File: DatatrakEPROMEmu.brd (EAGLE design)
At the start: 151.1 x 66 mm, 46 parts, among them IC1 LD1117AS33TR, IC2 XC95144XL_TQ144_P, Q1 BC847CSMD, Q2 BC847CSMD, Q3 BC847CSMD, U1 SN74LVCH16T245DGGR, U2 SN74LVCH16T245DGGR, U3 SN74LVCH16T245DGGR, U4 IS62WV25616DBLL-45TLI, U5 FT240XS, X1 MABC48B2, X2 PN61729-S

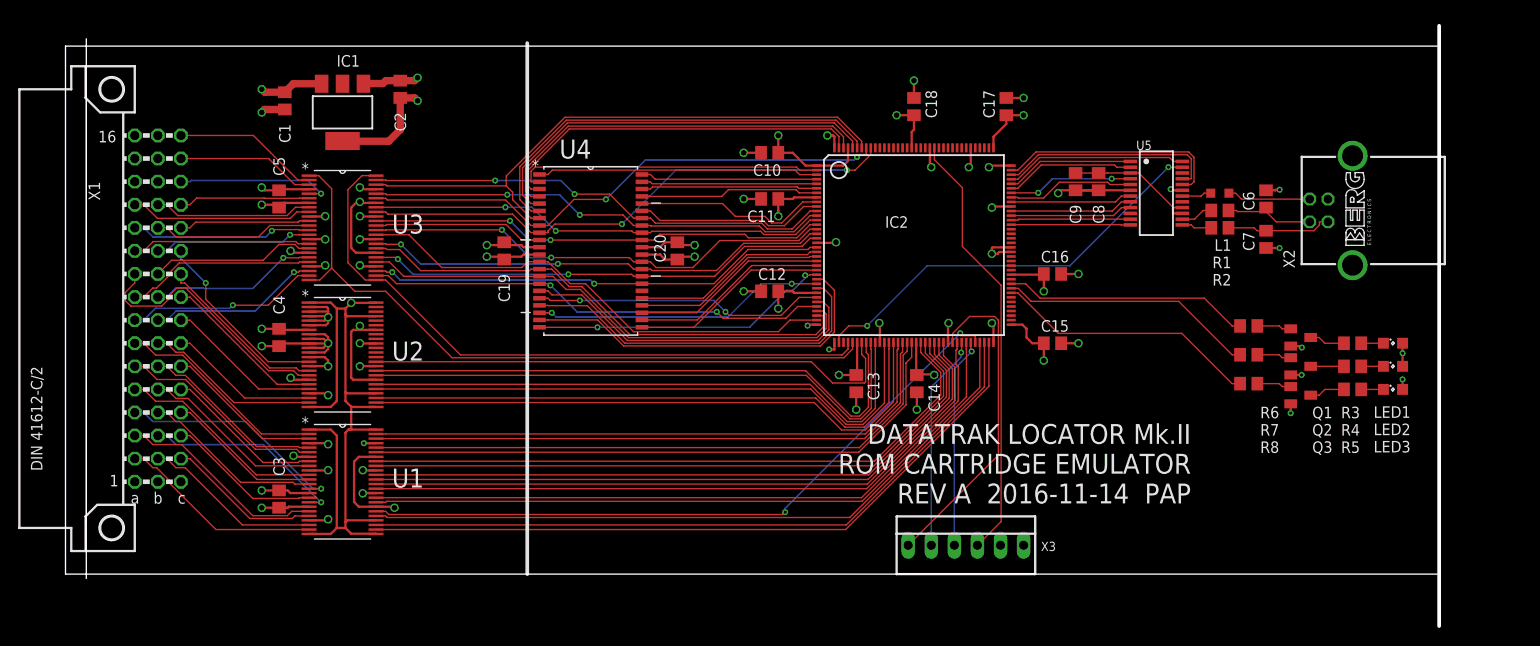
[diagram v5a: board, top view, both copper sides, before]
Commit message: remove right-side marker line
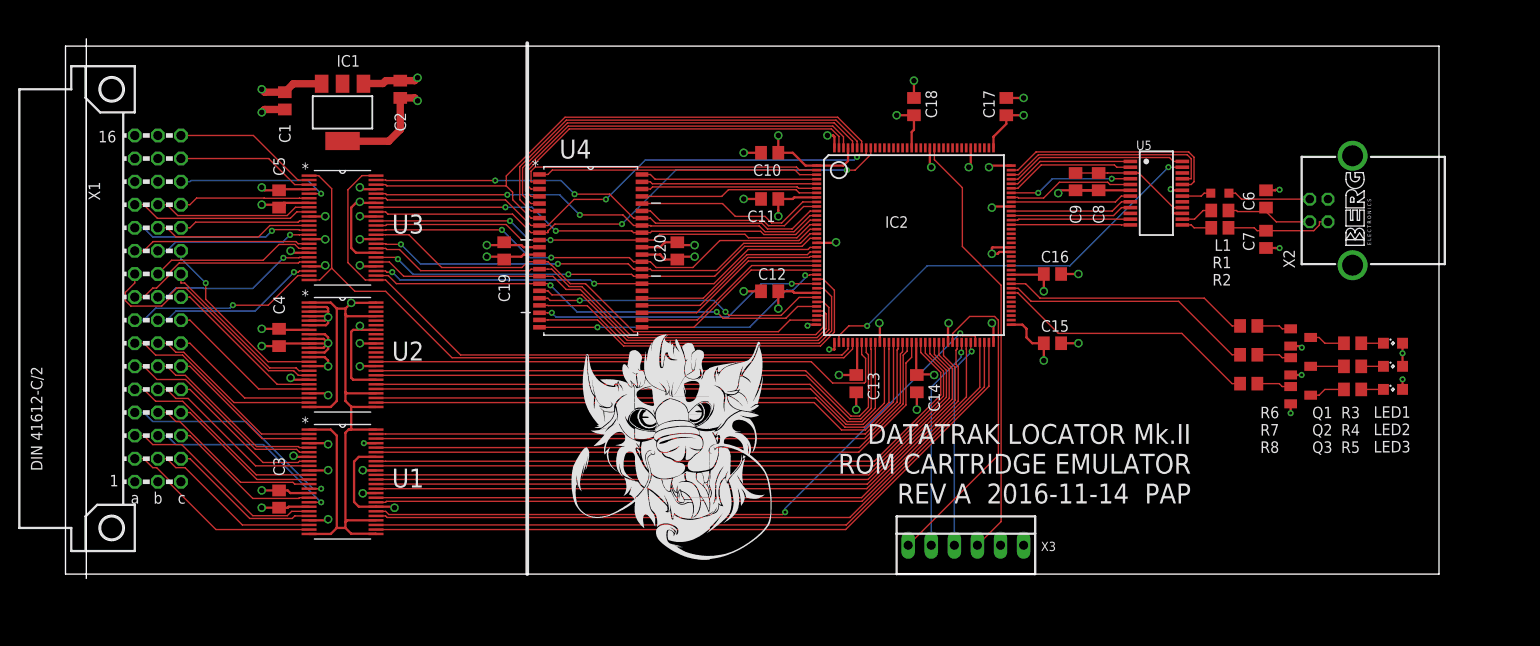
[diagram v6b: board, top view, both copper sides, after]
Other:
- board size 151.1 x 66 mm -> 151.1 x 58.1 mm
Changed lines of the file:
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@@
 <wire x1="0" y1="58.09" x2="0" y2="0" width="0" layer="20"/>
 <wire x1="50.8" y1="58.42" x2="50.8" y2="0" width="0.4064" layer="21"/>
-<wire x1="151.13" y1="60.325" x2="151.13" y2="-5.715" width="0.4064" layer="20"/>
 <text x="123.825" y="16.51" size="2.1844" layer="25" align="top-right">DATATRAK LOCATOR Mk.II
 ROM CARTRIDGE EMULATOR
@@
 </signal>
 </signals>
+<errors>
+</errors>
 </board>
 </drawing>
